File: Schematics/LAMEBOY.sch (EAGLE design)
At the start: 61 parts, among them IC1 PCF8574T, IC3 MCP73831, Q1 12MHz, U1 USD-SOCKETMICROSDEBAY, U2 USB

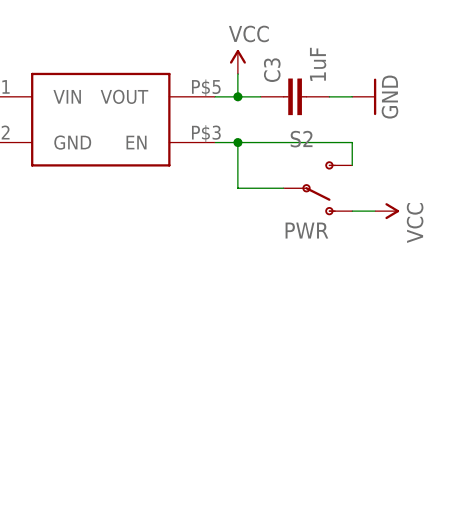
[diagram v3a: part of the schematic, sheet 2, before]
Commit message: wrong power for enabling regulator
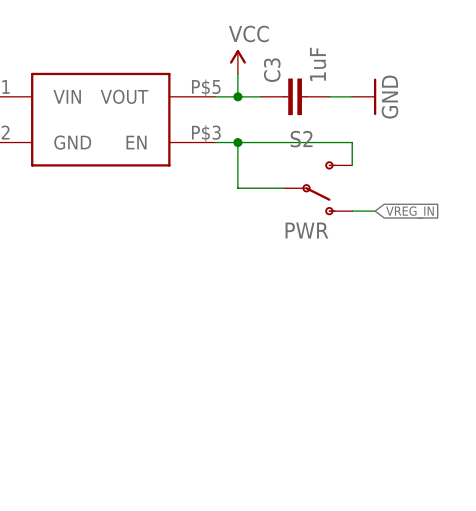
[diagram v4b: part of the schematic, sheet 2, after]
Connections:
- net VCC: no longer S2.O
- net VREG_IN: now also S2.O
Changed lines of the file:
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@@
 <part name="R11" library="rcl" deviceset="R-EU_" device="ONEFITSALL" value="470"/>
 <part name="GND22" library="supply1" deviceset="GND" device=""/>
-<part name="SUPPLY1" library="SparkFun-Aesthetics" deviceset="VCC" device=""/>
 <part name="U$6" library="SparkFun-DiscreteSemi" deviceset="MMDT3904" device="" value="BC847S"/>
 <part name="U$7" library="SparkFun-DiscreteSemi" deviceset="MMDT3904" device="" value="BC847S"/>
@@
 <instance part="C3" gate="G$1" x="154.94" y="66.04" rot="R90"/>
 <instance part="S2" gate="1" x="157.48" y="55.88" rot="MR180"/>
-<instance part="SUPPLY1" gate="G$1" x="165.1" y="53.34" rot="R270"/>
 <instance part="U$9" gate="G$1" x="134.62" y="63.5"/>
 <instance part="GND34" gate="1" x="119.38" y="55.88"/>
@@
 <wire x1="111.76" y1="66.04" x2="121.92" y2="66.04" width="0.1524" layer="91"/>
 </segment>
+<segment>
+<pinref part="S2" gate="1" pin="O"/>
+<wire x1="162.56" y1="53.34" x2="165.1" y2="53.34" width="0.1524" layer="91"/>
+<label x="165.1" y="53.34" size="1.016" layer="95" xref="yes"/>
+</segment>
 </net>
 <net name="VCC" class="0">
 <segment>
-<pinref part="S2" gate="1" pin="O"/>
-<pinref part="SUPPLY1" gate="G$1" pin="VCC"/>
-<wire x1="165.1" y1="53.34" x2="162.56" y2="53.34" width="0.1524" layer="91"/>
-</segment>
-<segment>
 <pinref part="U$9" gate="G$1" pin="VOUT"/>
